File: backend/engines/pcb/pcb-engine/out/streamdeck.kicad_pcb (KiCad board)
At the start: 2 copper layers, 89.8 x 92.5 mm, 27 parts, among them SW1 M1, SW10 M14, SW2 M2, SW3 M5, SW4 M6, SW5 M7, SW6 M9, SW7 M10, SW8 M11, SW9 M12, U1 XIAO RP2040

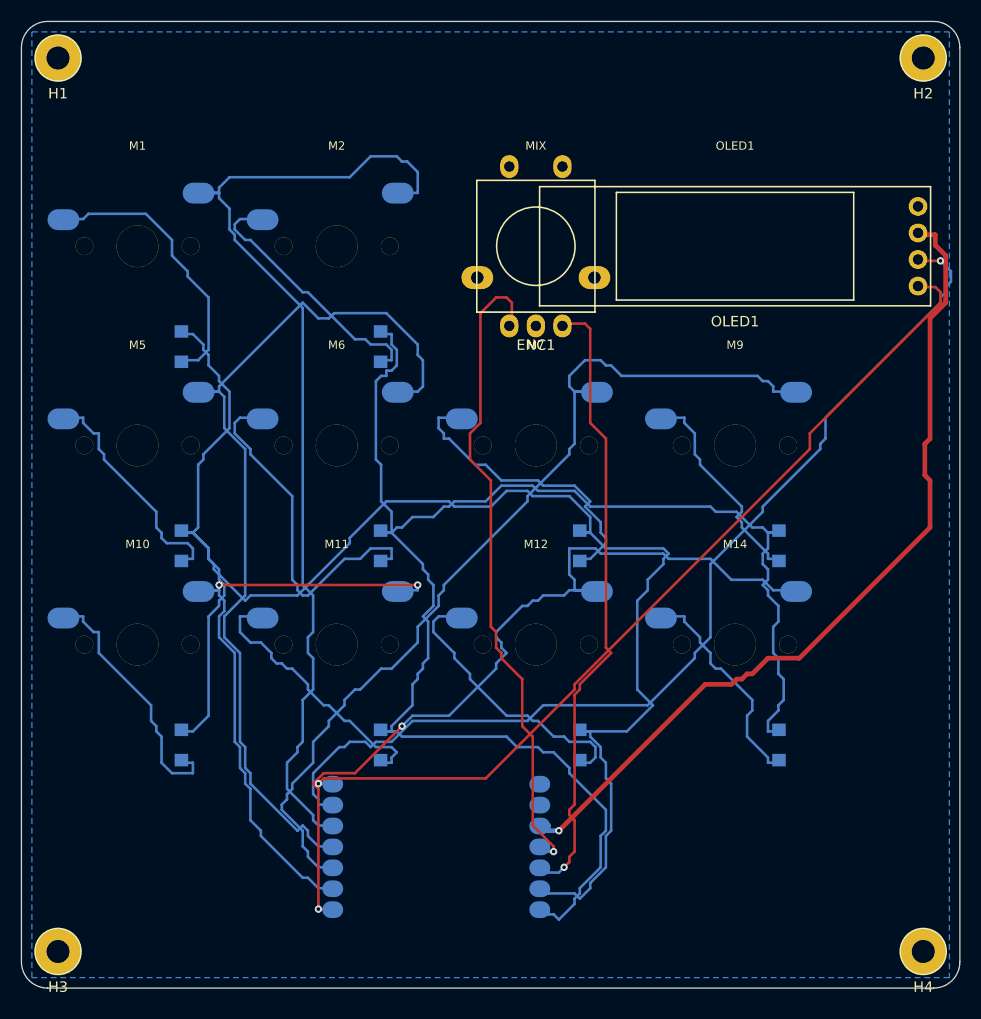
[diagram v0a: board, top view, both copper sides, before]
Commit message: case compiler: pcb result -> parametric openscad. xiao flipped 180 so usb faces the board edge. job #2 (ninepad) end to end with case artifacts. openscad-verified stls for all reference boards
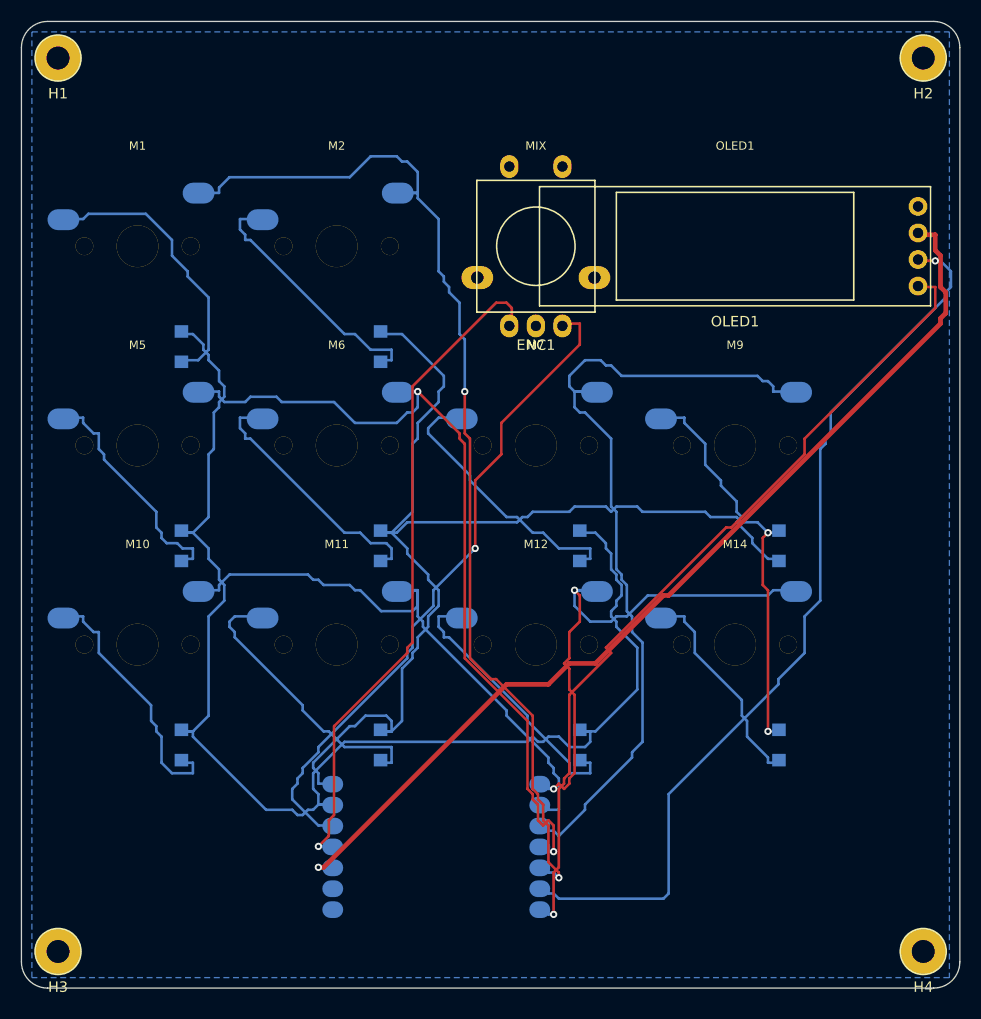
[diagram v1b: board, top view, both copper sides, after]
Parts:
- turned U1 to -180 degrees
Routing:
- net ROW0: track 156.1 -> 127.3 mm
- net COL4: track 80.6 -> 52.4 mm
- net ROW1: track 153.2 -> 127.6 mm, vias 0 -> 2
- net +3V3: track 81.0 -> 93.2 mm
- net N_SW4: track 34.3 -> 24.6 mm
- net COL2: track 90.3 -> 80.9 mm
- net SCL: track 96.7 -> 87.5 mm
- net COL1: track 87.4 -> 81.5 mm, vias 0 -> 2
- net COL0: track 97.8 -> 103.5 mm, vias 0 -> 2
- net SDA: track 84.4 -> 79.3 mm
- net ENC1_B: track 60.5 -> 63.4 mm
- net N_SW5: track 28.8 -> 26.3 mm
- net COL3: track 60.6 -> 58.2 mm, vias 2 -> 0
- net N_SW8: track 26.1 -> 27.1 mm
- net N_SW10: track 21.0 -> 20.3 mm
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
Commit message: the component geometry pipeline: one record, many projections
- CaseProjection on every FootprintDef (plateOpening, plateHole,
  plateWindow, plateThickness, usbShell) — the case engine consumes
  the registry, zero hardcoded component geometry left
- category-driven classification everywhere (case engine, netlist,
  bom, stats) — id-list filters removed
- CHOC_V1 copper fixed: was mx pin geometry (footprint drift), now
  verbatim from marbastlib SW_choc_v1_1u with provenance
- cell.switchType wired at the layout resolution joint; choc board
  routes (147 segs) + validates; choc case auto-defaults 1.2mm plate
  and 13.8x13.8 openings — propagation proven on a real ninepad
- streamdeck fixture fix (14 keys on 12 positions, v0 leftover)
- research: component-geometry-pipeline.md (sourcing chain: kicad
  defaults/marbastlib -> snappeda/componentsearchengine -> grabcad 3d)
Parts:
- SW10: value M14 -> M13
- SW6: value M9 -> M8
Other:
- board text added: "M13"
- board text added: "M8"
- board text removed: "M14"
- board text removed: "M9"
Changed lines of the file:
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@@
   (attr through_hole)
   (fp_text reference "SW6" (at 0 -8.2) (layer B.SilkS) (effects (font (size 1 1) (thickness 0.15))))
-  (fp_text value "M9" (at 0 8.2) (layer B.Fab) (effects (font (size 1 1) (thickness 0.15))))
+  (fp_text value "M8" (at 0 8.2) (layer B.Fab) (effects (font (size 1 1) (thickness 0.15))))
   (fp_line (start 6.7 -6.7) (end -6.7 -6.7) (stroke (width 0.15) (type solid)) (fill solid) (layer B.SilkS))
   (fp_line (start -6.7 -6.7) (end -6.7 6.7) (stroke (width 0.15) (type solid)) (fill solid) (layer B.SilkS))
@@
   (attr through_hole)
   (fp_text reference "SW10" (at 0 -8.2) (layer B.SilkS) (effects (font (size 1 1) (thickness 0.15))))
-  (fp_text value "M14" (at 0 8.2) (layer B.Fab) (effects (font (size 1 1) (thickness 0.15))))
+  (fp_text value "M13" (at 0 8.2) (layer B.Fab) (effects (font (size 1 1) (thickness 0.15))))
   (fp_line (start 6.7 -6.7) (end -6.7 -6.7) (stroke (width 0.15) (type solid)) (fill solid) (layer B.SilkS))
   (fp_line (start -6.7 -6.7) (end -6.7 6.7) (stroke (width 0.15) (type solid)) (fill solid) (layer B.SilkS))
@@
   (gr_text "M6" (at -14.725 -15.275) (layer F.SilkS) (effects (font (size 0.8 0.8) (thickness 0.15))))
   (gr_text "M7" (at 4.325 -15.275) (layer F.SilkS) (effects (font (size 0.8 0.8) (thickness 0.15))))
-  (gr_text "M9" (at 23.375 -15.275) (layer F.SilkS) (effects (font (size 0.8 0.8) (thickness 0.15))))
+  (gr_text "M8" (at 23.375 -15.275) (layer F.SilkS) (effects (font (size 0.8 0.8) (thickness 0.15))))
   (gr_text "M10" (at -33.775 3.775) (layer F.SilkS) (effects (font (size 0.8 0.8) (thickness 0.15))))
   (gr_text "M11" (at -14.725 3.775) (layer F.SilkS) (effects (font (size 0.8 0.8) (thickness 0.15))))
   (gr_text "M12" (at 4.325 3.775) (layer F.SilkS) (effects (font (size 0.8 0.8) (thickness 0.15))))
-  (gr_text "M14" (at 23.375 3.775) (layer F.SilkS) (effects (font (size 0.8 0.8) (thickness 0.15))))
+  (gr_text "M13" (at 23.375 3.775) (layer F.SilkS) (effects (font (size 0.8 0.8) (thickness 0.15))))
   (gr_text "keeberia-streamdeck" (at 0 44.625) (layer B.SilkS) (effects (font (size 1 1) (thickness 0.15))))
 )
